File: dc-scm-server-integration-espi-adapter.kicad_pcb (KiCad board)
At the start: 8 copper layers, 62 x 87 mm, 232 parts, among them J1 PinHeader_2x6_P2.54mm_Drill1.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, J10 PinHeader_2x5_P1.27mm_SMD, J11 PinHeader_2x5_P1.27mm_SMD, J12 PinHeader_2x5_P1.27mm_SMD, J13 Tag-Connect_TC2050-IDC-NL_2x5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, J14 Tag-Connect_TC2050-IDC-NL_2x5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, J15 USB-C_GCT_USB4105-GF-A, J2 PinHeader_2x5_P1.27mm_SMD, J3 PinHeader_2x5_P1.27mm_SMD, J4 PinHeader_2x5_P1.27mm_SMD, J5 PinHeader_2x5_P1.27mm_SMD, J6 PinHeader_2x5_P1.27mm_SMD, J7 PinHeader_2x5_P1.27mm_SMD, J8 PinHeader_2x5_P1.27mm_SMD, J9 PinHeader_2x5_P1.27mm_SMD, Q1 DMG1012T-7, SW1 SW_KSC441J70SHLFS_SMD, SW2 SW_KSC441J70SHLFS_SMD, SW3 SW_KSC441J70SHLFS_SMD, U1 MEC1723N-B0-I/SZ, U2 TLV76701_WSON, U3 AP62301_TSOT, U4 MT25QU01GBBB8_SOIC, U5 SN74AC7541_VQFN, U6 SN74AC7541_VQFN, U7 FT2232HL-REEL, Y1 Resonator_32.768kHz_ECX-31B, Y2 Resonator_12MHz_KX-7

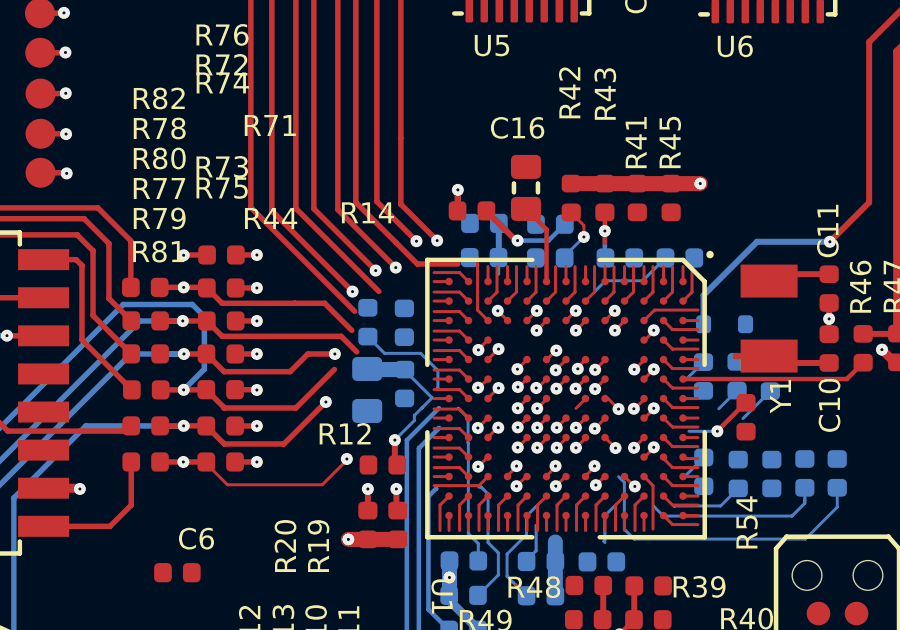
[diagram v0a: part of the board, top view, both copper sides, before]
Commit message: [#103697] pcb: reduce GND pur min width and spacing to 0.125mm
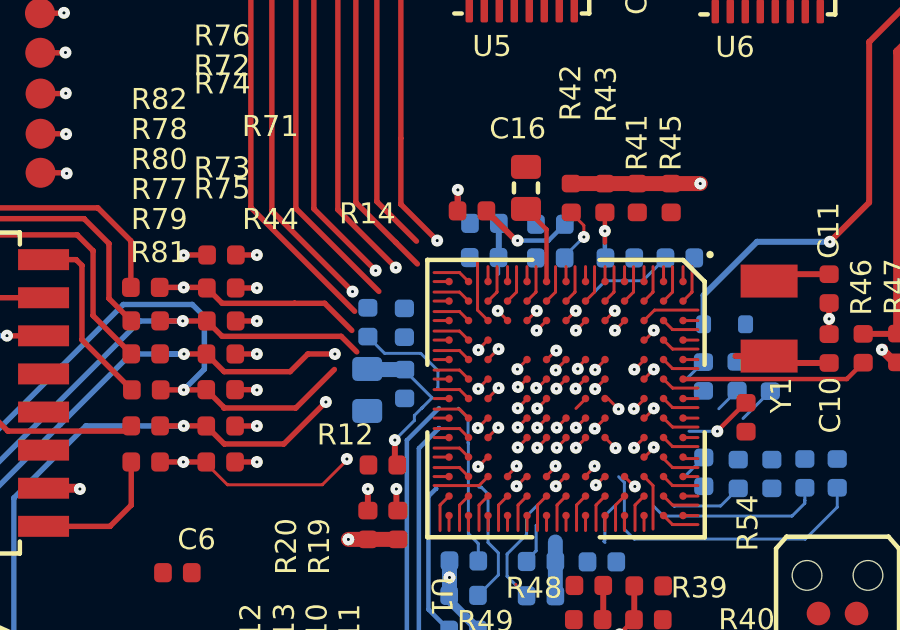
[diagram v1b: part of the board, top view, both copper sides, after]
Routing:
- net /DC-SCM Interposer connector/EC_ESPI.~{CS0}: track 47.8 -> 46.4 mm
- net /DC-SCM Interposer connector/EC_ESPI.IO0: vias 3 -> 2
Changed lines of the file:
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@@
 		(net "/DC-SCM Interposer connector/EC_ESPI.~{CS0}")
 	)
-	(segment
-		(start 76.8 99.8)
-		(end 75.45 99.8)
-		(width 0.182)
-		(layer "F.Cu")
-		(net "/DC-SCM Interposer connector/EC_ESPI.~{CS0}")
-	)
 	(via
 		(at 72.9 71.73)
@@
 	)
 	(segment
-		(start 77.805467 103.626213)
-		(end 77.509156 103.922524)
+		(start 77.480467 103.961213)
+		(end 77.509156 103.932524)
 		(width 0.1)
 		(layer "F.Cu")
@@
 	)
 	(segment
+		(start 77.509156 103.932524)
+		(end 77.509156 103.922524)
+		(width 0.1)
+		(layer "F.Cu")
+		(net "/Flash/EC_QSPI.IO2")
+	)
+	(segment
 		(start 77.509156 103.922524)
-		(end 77.472798 103.922524)
+		(end 77.805467 103.626213)
 		(width 0.1)
 		(layer "F.Cu")
@@
 	)
 	(via
-		(at 77.472798 103.922524)
+		(at 77.480467 103.961213)
 		(size 0.4)
 		(drill 0.1)
@@
 	)
 	(segment
-		(start 75.16 104.28)
-		(end 73.22 106.22)
-		(width 0.1)
-		(layer "In2.Cu")
-		(net "/Flash/EC_QSPI.IO2")
-	)
-	(segment
 		(start 73.22 106.22)
 		(end 73.16 106.28)
@@
 	)
 	(segment
-		(start 77.472798 103.922524)
-		(end 77.115322 104.28)
+		(start 77.480467 103.961213)
+		(end 77.434109 103.961213)
 		(width 0.1)
 		(layer "In2.Cu")
@@
 	)
 	(segment
-		(start 77.115322 104.28)
-		(end 75.16 104.28)
+		(start 77.434109 103.961213)
+		(end 77.115322 104.28)
 		(width 0.1)
 		(layer "In2.Cu")
@@
 	)
 	(segment
+		(start 77.115322 104.28)
+		(end 75.16 104.28)
+		(width 0.1)
+		(layer "In2.Cu")
+		(net "/Flash/EC_QSPI.IO2")
+	)
+	(segment
+		(start 75.16 104.28)
+		(end 73.22 106.22)
+		(width 0.1)
+		(layer "In2.Cu")
+		(net "/Flash/EC_QSPI.IO2")
+	)
+	(segment
 		(start 64.31 96.78)
 		(end 64.53 97)
@@
 	)
 	(via
-		(at 75.42 99.04)
-		(size 0.4)
-		(drill 0.1)
-		(layers "F.Cu" "B.Cu")
-		(net "/DC-SCM Interposer connector/EC_ESPI.IO0")
-	)
-	(via
 		(at 67.43 61.4)
 		(size 0.4)
@@
 		(hatch edge 0.1)
 		(connect_pads yes
-			(clearance 0.25)
+			(clearance 0.125)
 		)
-		(min_thickness 0.25)
+		(min_thickness 0.125)
 		(fill yes
 			(thermal_gap 0.5)
